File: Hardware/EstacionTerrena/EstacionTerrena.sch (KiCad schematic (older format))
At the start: 7 parts, among them J1 5-1814832-1, J3 Conn_01x03

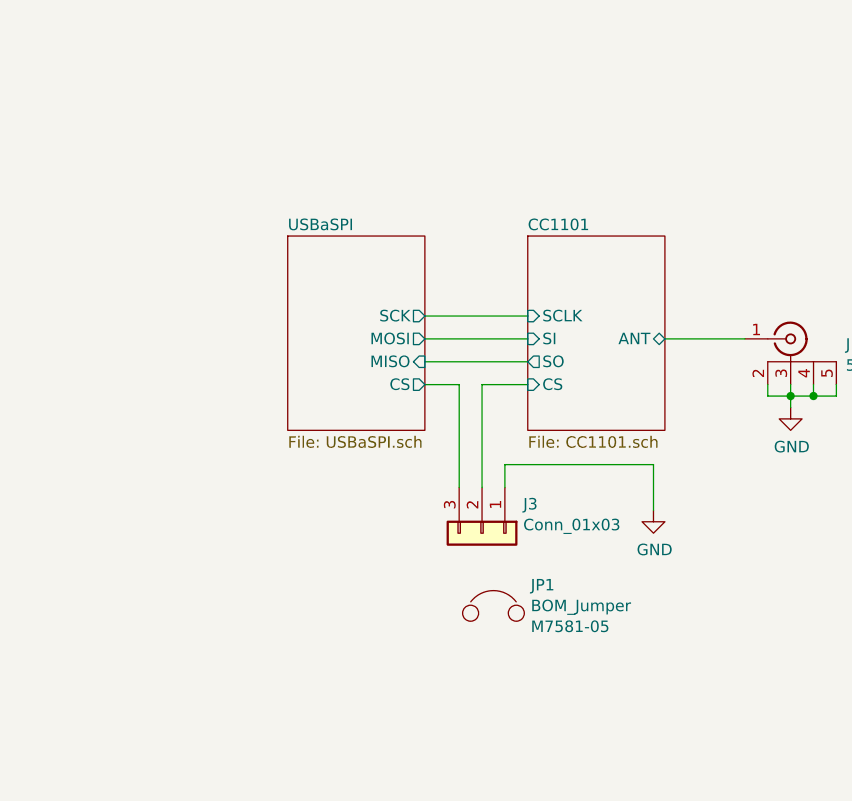
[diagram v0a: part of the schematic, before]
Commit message: Agregados testpoint a Estacion terrena y modificado jumper de CS
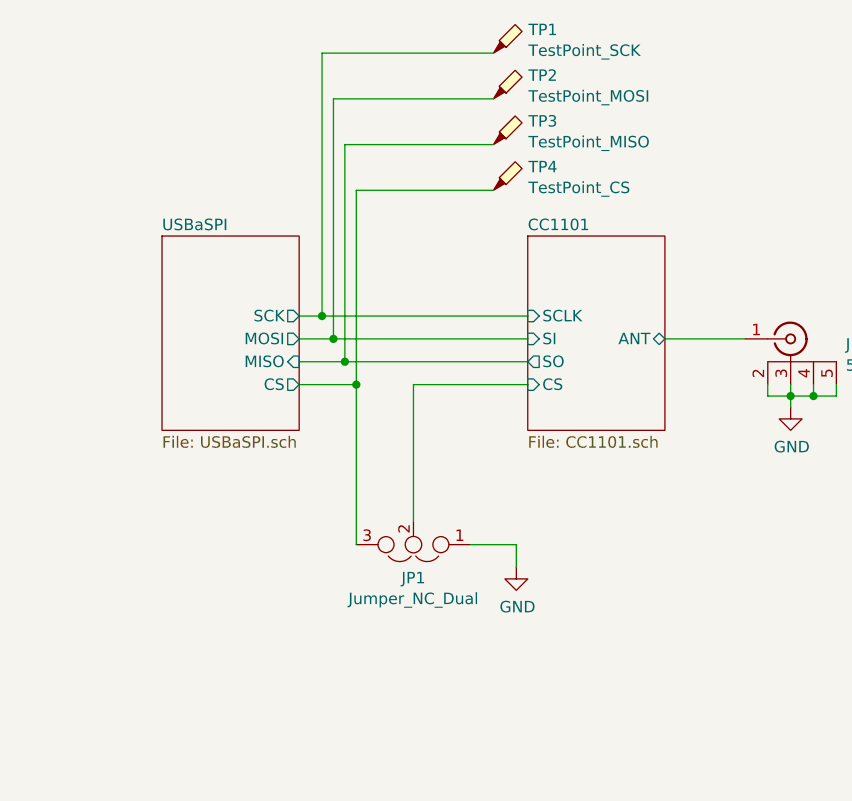
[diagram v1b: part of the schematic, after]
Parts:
- removed J3: Conn_01x03, Connector_PinHeader_2.54mm:PinHeader_1x03_P2.54mm_Horizontal, symbol Connector_Generic:Conn_01x03
- removed JP1: BOM_Jumper, AXTEC:Empty_Footprint, symbol AXTEC_IC:BOM_Jumper
- added JP1: Jumper_NC_Dual, Jumper:SolderJumper-3_P1.3mm_Open_RoundedPad1.0x1.5mm_NumberLabels, symbol Device:Jumper_NC_Dual
- added TP1: TestPoint_SCK, TestPoint:TestPoint_Pad_D1.0mm, symbol Connector:TestPoint_Probe
- added TP2: TestPoint_MOSI, TestPoint:TestPoint_Pad_D1.0mm, symbol Connector:TestPoint_Probe
- added TP3: TestPoint_MISO, TestPoint:TestPoint_Pad_D1.0mm, symbol Connector:TestPoint_Probe
- added TP4: TestPoint_CS, TestPoint:TestPoint_Pad_D1.0mm, symbol Connector:TestPoint_Probe
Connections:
- net CC1101/CS: now also JP1.2
- net CC1101/SCLK: now also TP1.1
- net CC1101/SI: now also TP2.1
- net CC1101/SO: now also TP3.1
- net GND: now also JP1.1
- net USBaSPI/CS: now also JP1.3, TP4.1
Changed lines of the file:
@@
 $EndDescr
 $Sheet
-S 5050 3600 600  850
+S 4500 3600 600  850
 U 5B9997DB
 F0 "USBaSPI" 50
 F1 "USBaSPI.sch" 50
-F2 "MOSI" O R 5650 4050 50
-F3 "SCK" O R 5650 3950 50
-F4 "MISO" I R 5650 4150 50
-F5 "CS" O R 5650 4250 50
+F2 "MOSI" O R 5100 4050 50
+F3 "SCK" O R 5100 3950 50
+F4 "MISO" I R 5100 4150 50
+F5 "CS" O R 5100 4250 50
 $EndSheet
 $Sheet
@@
 F6 "CS" I L 6100 4250 50
 $EndSheet
-Wire Wire Line
-	5650 3950 6100 3950
-Wire Wire Line
-	5650 4050 6100 4050
-Wire Wire Line
-	5650 4150 6100 4150
 $Comp
 L power:GND #PWR01
@@
 $EndComp
 $Comp
-L Connector_Generic:Conn_01x03 J3
-U 1 1 5C00A33C
-P 5900 4900
-F 0 "J3" V 5773 5080 50  0000 L CNN
-F 1 "Conn_01x03" V 5864 5080 50  0000 L CNN
-F 2 "Connector_PinHeader_2.54mm:PinHeader_1x03_P2.54mm_Horizontal" H 5900 4900 50  0001 C CNN
-F 3 "~" H 5900 4900 50  0001 C CNN
-F 4 "61300311121" V 5900 4900 50  0001 C CNN "Manufacturer Part Number"
-	1    5900 4900
-	0    1    1    0
-$EndComp
-Wire Wire Line
-	5650 4250 5800 4250
-Wire Wire Line
-	5800 4250 5800 4700
-Wire Wire Line
-	6100 4250 5900 4250
-Wire Wire Line
-	5900 4250 5900 4700
-$Comp
 L power:GND #PWR026
 U 1 1 5C00A55B
-P 6650 4800
-F 0 "#PWR026" H 6650 4550 50  0001 C CNN
-F 1 "GND" H 6655 4627 50  0000 C CNN
-F 2 "" H 6650 4800 50  0001 C CNN
-F 3 "" H 6650 4800 50  0001 C CNN
-	1    6650 4800
-	1    0    0    -1
-$EndComp
-Wire Wire Line
-	6000 4700 6000 4600
-Wire Wire Line
-	6000 4600 6650 4600
-Wire Wire Line
-	6650 4600 6650 4800
-$Comp
-L AXTEC_IC:BOM_Jumper JP1
-U 1 1 5C00354F
-P 5950 5200
-F 0 "JP1" H 6113 5273 50  0000 L CNN
-F 1 "BOM_Jumper" H 6113 5182 50  0000 L CNN
-F 2 "AXTEC:Empty_Footprint" H 5950 5300 50  0001 C CNN
-F 3 "" H 5950 5300 50  0001 C CNN
-F 4 "M7581-05" H 6113 5091 50  0000 L CNN "Manufacturer Part Number"
-	1    5950 5200
-	1    0    0    -1
-$EndComp
+P 6050 5050
+F 0 "#PWR026" H 6050 4800 50  0001 C CNN
+F 1 "GND" H 6055 4877 50  0000 C CNN
+F 2 "" H 6050 5050 50  0001 C CNN
+F 3 "" H 6050 5050 50  0001 C CNN
+	1    6050 5050
+	1    0    0    -1
+$EndComp
+Wire Wire Line
+	5100 3950 5200 3950
+$Comp
+L Connector:TestPoint_Probe TP4
+U 1 1 5C2D7A58
+P 5950 3400
+F 0 "TP4" H 6103 3502 50  0000 L CNN
+F 1 "TestPoint_CS" H 6103 3411 50  0000 L CNN
+F 2 "TestPoint:TestPoint_Pad_D1.0mm" H 6150 3400 50  0001 C CNN
+F 3 "~" H 6150 3400 50  0001 C CNN
+	1    5950 3400
+	1    0    0    -1
+$EndComp
+$Comp
+L Connector:TestPoint_Probe TP3
+U 1 1 5C2D7AA0
+P 5950 3200
+F 0 "TP3" H 6103 3302 50  0000 L CNN
+F 1 "TestPoint_MISO" H 6103 3211 50  0000 L CNN
+F 2 "TestPoint:TestPoint_Pad_D1.0mm" H 6150 3200 50  0001 C CNN
+F 3 "~" H 6150 3200 50  0001 C CNN
+	1    5950 3200
+	1    0    0    -1
+$EndComp
+$Comp
+L Connector:TestPoint_Probe TP2
+U 1 1 5C2D7ACA
+P 5950 3000
+F 0 "TP2" H 6103 3102 50  0000 L CNN
+F 1 "TestPoint_MOSI" H 6103 3011 50  0000 L CNN
+F 2 "TestPoint:TestPoint_Pad_D1.0mm" H 6150 3000 50  0001 C CNN
+F 3 "~" H 6150 3000 50  0001 C CNN
+	1    5950 3000
+	1    0    0    -1
+$EndComp
+$Comp
+L Connector:TestPoint_Probe TP1
+U 1 1 5C2D7B04
+P 5950 2800
+F 0 "TP1" H 6103 2902 50  0000 L CNN
+F 1 "TestPoint_SCK" H 6103 2811 50  0000 L CNN
+F 2 "TestPoint:TestPoint_Pad_D1.0mm" H 6150 2800 50  0001 C CNN
+F 3 "~" H 6150 2800 50  0001 C CNN
+	1    5950 2800
+	1    0    0    -1
+$EndComp
+Wire Wire Line
+	5600 4250 6100 4250
+Wire Wire Line
+	5100 4250 5350 4250
+Wire Wire Line
+	5200 3950 5200 2800
+Wire Wire Line
+	5200 2800 5950 2800
+Connection ~ 5200 3950
+Wire Wire Line
+	5200 3950 6100 3950
+$Comp
+L Device:Jumper_NC_Dual JP1
+U 1 1 5C2DD6B3
+P 5600 4950
+F 0 "JP1" H 5600 5096 50  0000 C CNN
+F 1 "Jumper_NC_Dual" H 5600 5187 50  0000 C CNN
+F 2 "Jumper:SolderJumper-3_P1.3mm_Open_RoundedPad1.0x1.5mm_NumberLabels" H 5600 4950 50  0001 C CNN
+F 3 "~" H 5600 4950 50  0001 C CNN
+	1    5600 4950
+	-1   0    0    1
+$EndComp
+Wire Wire Line
+	5350 4950 5350 4250
+Connection ~ 5350 4250
+Wire Wire Line
+	5600 4250 5600 4850
+Wire Wire Line
+	5850 4950 6050 4950
+Wire Wire Line
+	6050 4950 6050 5050
+Wire Wire Line
+	5100 4050 5250 4050
+Wire Wire Line
+	5100 4150 5300 4150
+Wire Wire Line
+	5300 4150 5300 3200
+Wire Wire Line
+	5300 3200 5950 3200
+Connection ~ 5300 4150
+Wire Wire Line
+	5300 4150 6100 4150
+Wire Wire Line
+	5250 4050 5250 3000
+Wire Wire Line
+	5250 3000 5950 3000
+Connection ~ 5250 4050
+Wire Wire Line
+	5250 4050 6100 4050
+Wire Wire Line
+	5350 4250 5350 3400
+Wire Wire Line
+	5350 3400 5950 3400
 $EndSCHEMATC
